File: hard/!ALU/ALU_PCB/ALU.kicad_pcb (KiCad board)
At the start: 2 copper layers, 99.1 x 99.1 mm, 37 parts, among them J1 Conn_01x09_Male, J11 Conn_01x01_Male, J12 Conn_01x01_Male, J13 Conn_01x01_Male, J14 Conn_01x01_Male, J2 Conn_01x09_Male, J25 Conn_01x01_Male, J26 Conn_01x01_Male, J27 Conn_01x01_Male, J28 Conn_01x01_Male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

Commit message: KiCAD 5 -> 9
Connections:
- net /~ADDx renamed /~{ADDx}
- net /~AND renamed /~{AND}
- net /~LSRx renamed /~{LSRx}
- net /~MOV renamed /~{MOV}
- net /~OR renamed /~{OR}
- net /~RSRV renamed /~{RSRV}
- net /~SWAP renamed /~{SWAP}
- net /~XOR renamed /~{XOR}
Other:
- net class Default removed
- board text added: "~{ADDx}"
- board text added: "~{AND}"
- board text added: "~{LSRx}"
- board text added: "~{MOV}"
- board text added: "~{OR}"
- board text added: "~{RSRV}"
- board text added: "~{SWAP}"
- board text added: "~{XOR}"
- board text removed: "~ADDx"
- board text removed: "~AND"
- board text removed: "~LSRx"
- board text removed: "~MOV"
- board text removed: "~OR"
- board text removed: "~RSRV"
- board text removed: "~SWAP"
- board text removed: "~XOR"

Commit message: ALU in work
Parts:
- moved J4 56.1 mm to (15.2, 101.6)
- moved R3 15.9 mm to (58.4, 92.7)
- moved U3 5.08 mm to (73.7, 22.9)
- moved J26 3.81 mm to (82.5, 110.5)
- moved U4 3.81 mm to (85.1, 22.9)
- moved J27 2.54 mm to (78.7, 110.5)
- moved U5 2.54 mm to (96.5, 22.9)
- moved J7 1.91 mm to (66.7, 110.2)
- moved Q1 1.91 mm to (69.2, 106.4)
- moved C1 1.27 mm to (67.3, 95.2)
- moved U6 1.27 mm to (108.0, 24.1)
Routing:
- net /Latch: track 87.3 -> 98.7 mm
- net GND: track 218.4 -> 210.3 mm
- net /CMP.Expand: track 16.5 -> 14.0 mm
- net /~{OR}: track 14.0 -> 16.5 mm
- net /O2: track 98.6 -> 97.3 mm
- net /A1: track 97.6 -> 96.3 mm
- net /O7: track 98.6 -> 97.3 mm
- net /B5: track 67.0 -> 65.7 mm
- net /A7: track 97.6 -> 96.3 mm
- net /A6: track 97.6 -> 96.3 mm
- net /A5: track 97.6 -> 96.3 mm
- net /A0: track 97.6 -> 96.3 mm
- net /O6: track 98.6 -> 97.3 mm
- net /O5: track 98.6 -> 97.3 mm
- net /O3: track 98.6 -> 97.3 mm
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
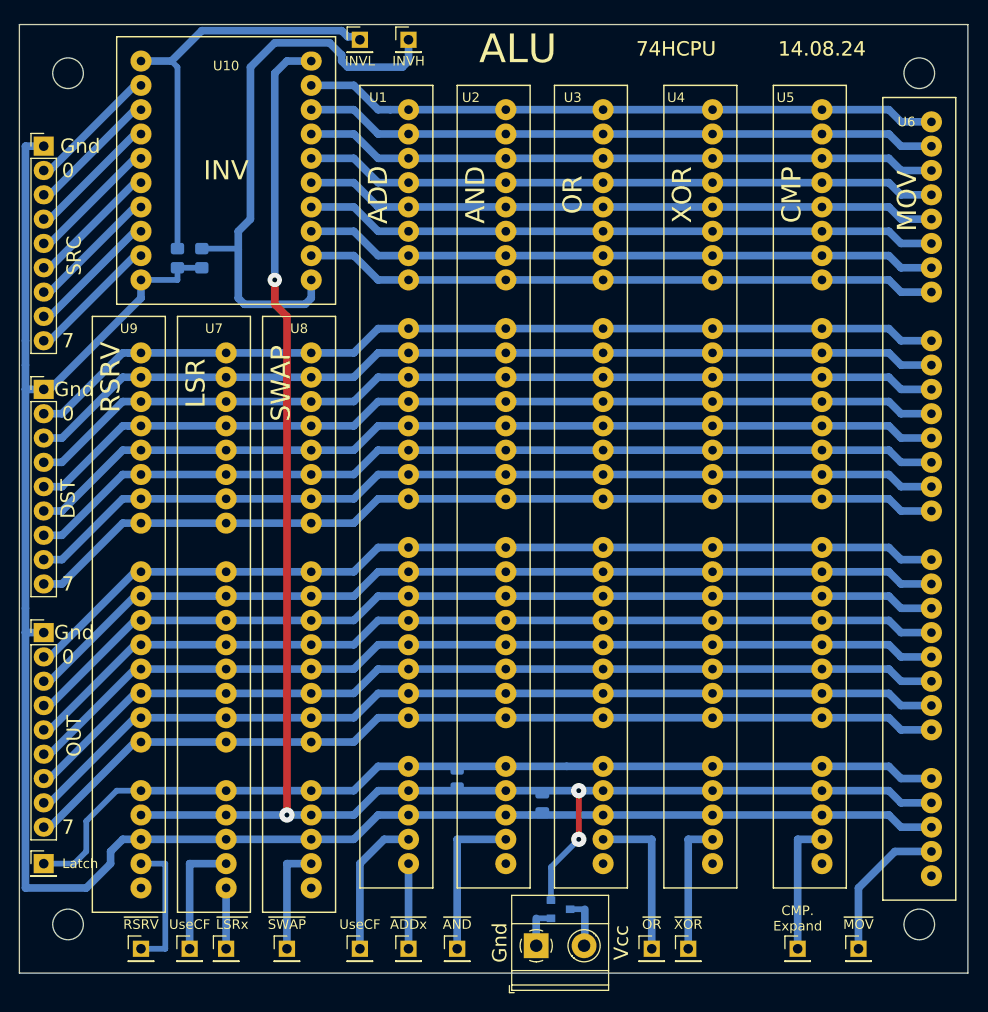
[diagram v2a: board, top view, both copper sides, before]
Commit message: Replace AND/OR/XOR/MOV on proper symbol
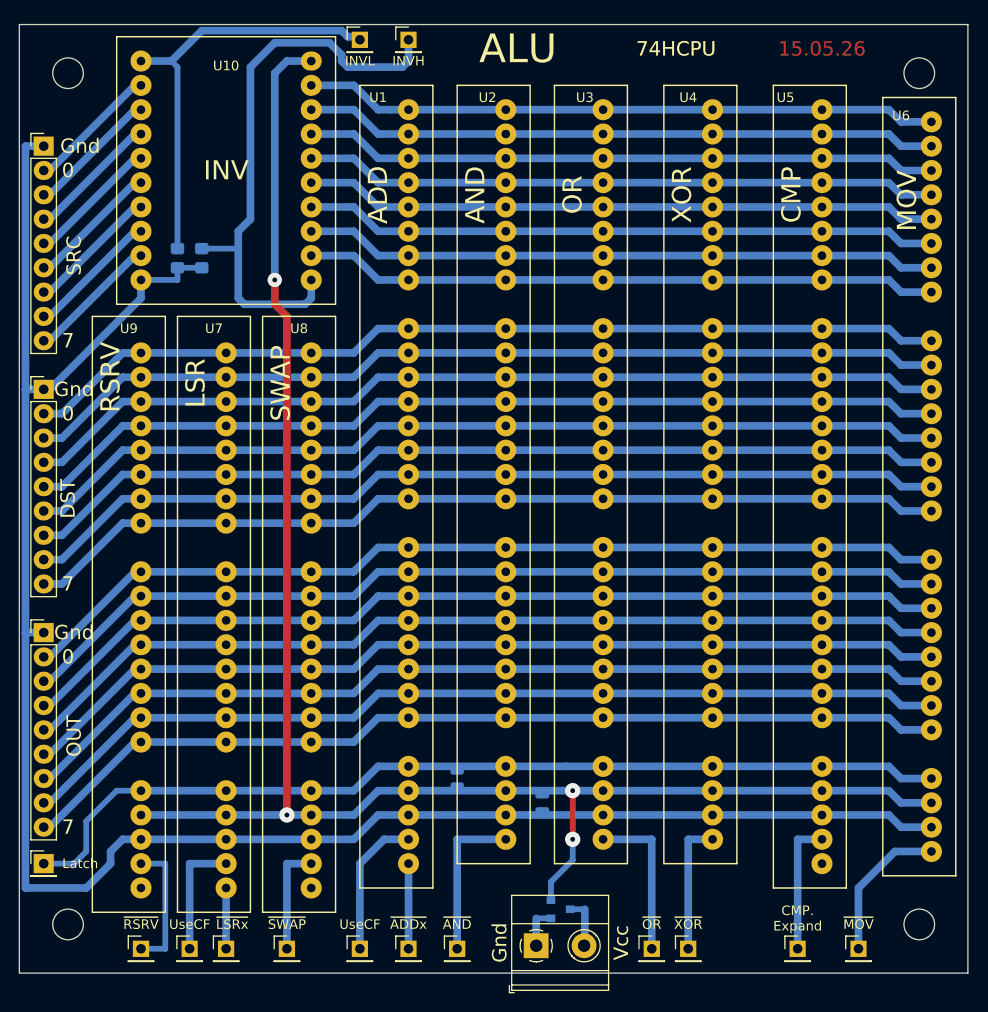
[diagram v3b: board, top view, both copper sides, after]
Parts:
- U2, U3, U4, U6: value CMD -> CMD1; footprint CommonLibrary:CMD -> Common:CMDwoC
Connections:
- U5 pad 29: Net-(U5-Pad29) -> unconnected-(U5-~{OE(C})-Pad29)
- U8 pad 21: Net-(U8-Pad21) -> unconnected-(U8-~{OE}-Pad21)
- U9 pad 21: Net-(U9-Pad21) -> unconnected-(U9-~{OE}-Pad21)
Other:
- board text added: "15.05.26"
- board text removed: "14.08.24"
